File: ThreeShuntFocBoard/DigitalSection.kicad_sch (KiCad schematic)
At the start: 16 parts, among them J1 Conn_01x05, J2 Conn_02x03_Odd_Even, J5 Conn_01x05

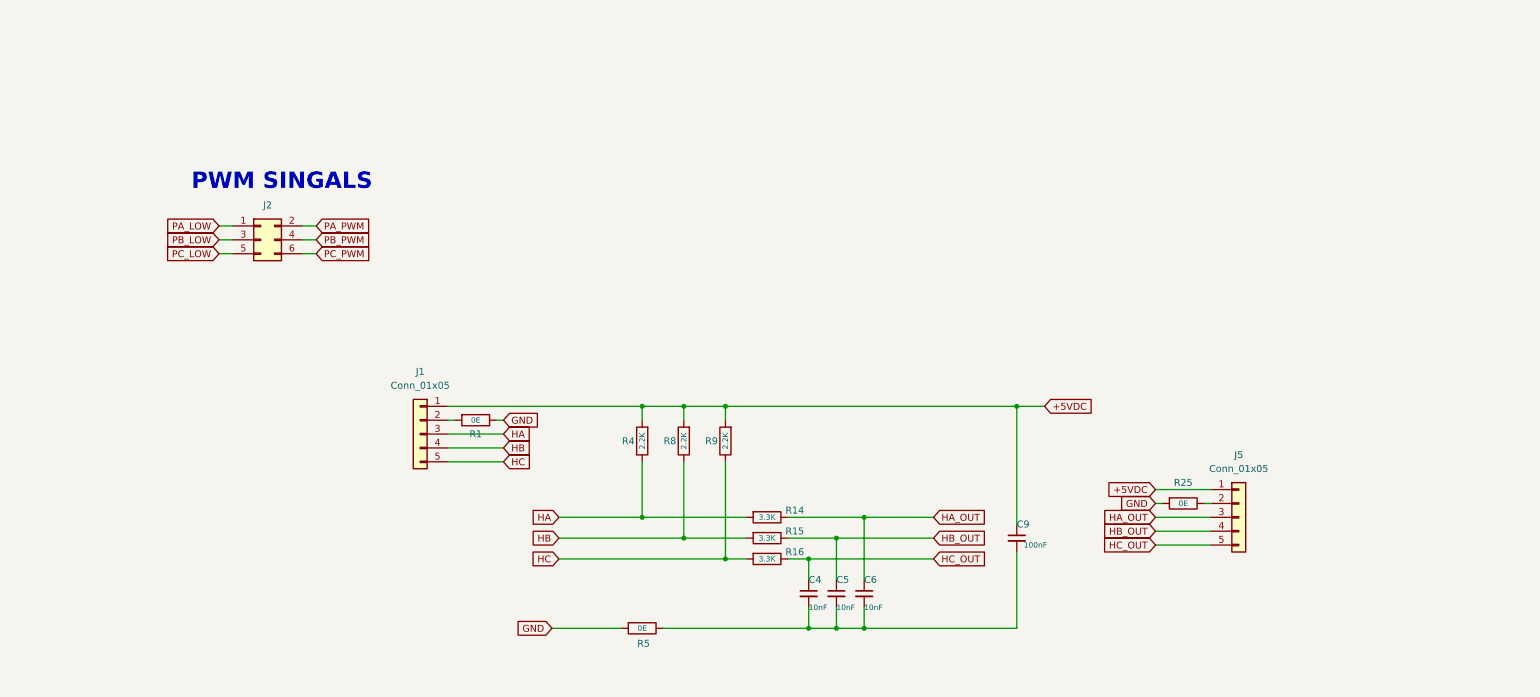
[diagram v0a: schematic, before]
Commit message: commit 2:  Updated Power Supply, Safety Fuse, Phase Design, and Hall Sensor Circuit
for more details read ChangesDetial.txt in same folder.
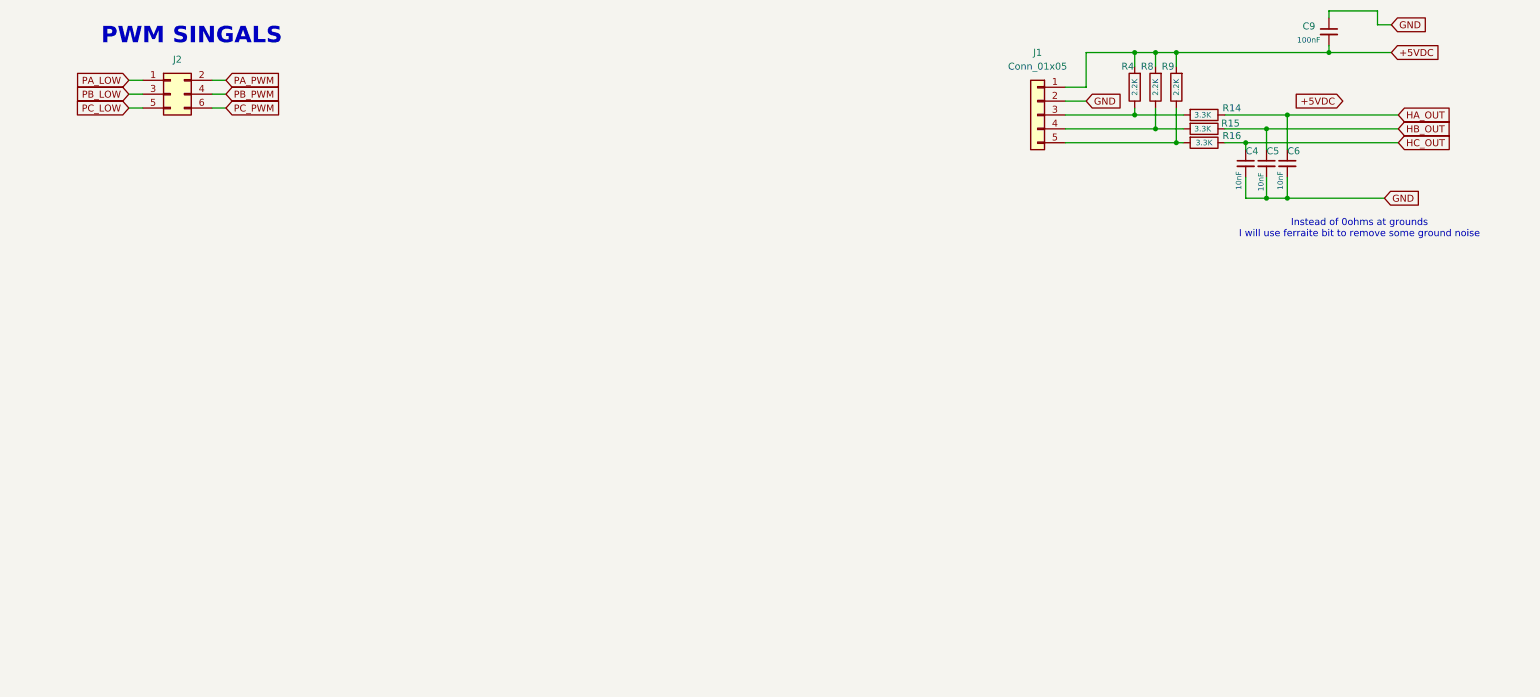
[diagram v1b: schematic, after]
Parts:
- removed J5: Conn_01x05, BLDC:Socket_Strip_Straight_1x05_Pitch2.54mm, symbol Connector_Generic:Conn_01x05
- removed R1, R25, R5: 0E, Footprints:R_0603, symbol Device:R
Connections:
- net +5VDC: now also C9.2; no longer C9.1
- net GND: now also C4.2, C5.2, C6.2, C9.1, J1.2 (Pin_2)
- net HA: no longer names the net of J1.3 (Pin_3), R14.2, R4.1
- net HB: no longer names the net of J1.4 (Pin_4), R15.2, R8.1
- net HC: no longer names the net of J1.5 (Pin_5), R16.2, R9.1
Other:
- note added: "Instead of 0ohms at grounds I will use ferraite bit to remove some ground noise"
- moved on the sheet: C4, C5, C6, C9, J1, J2, R14, R15, R16, R4, R8, R9

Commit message: Commit 3: Assigned STM32G431C6Tx (LQFP-48) pins as per the shared Excel, peripheral connections WIP, Phase C current sensing removed due to ADC group limitations
read attach excel files and changesDetails.txt file for more detail
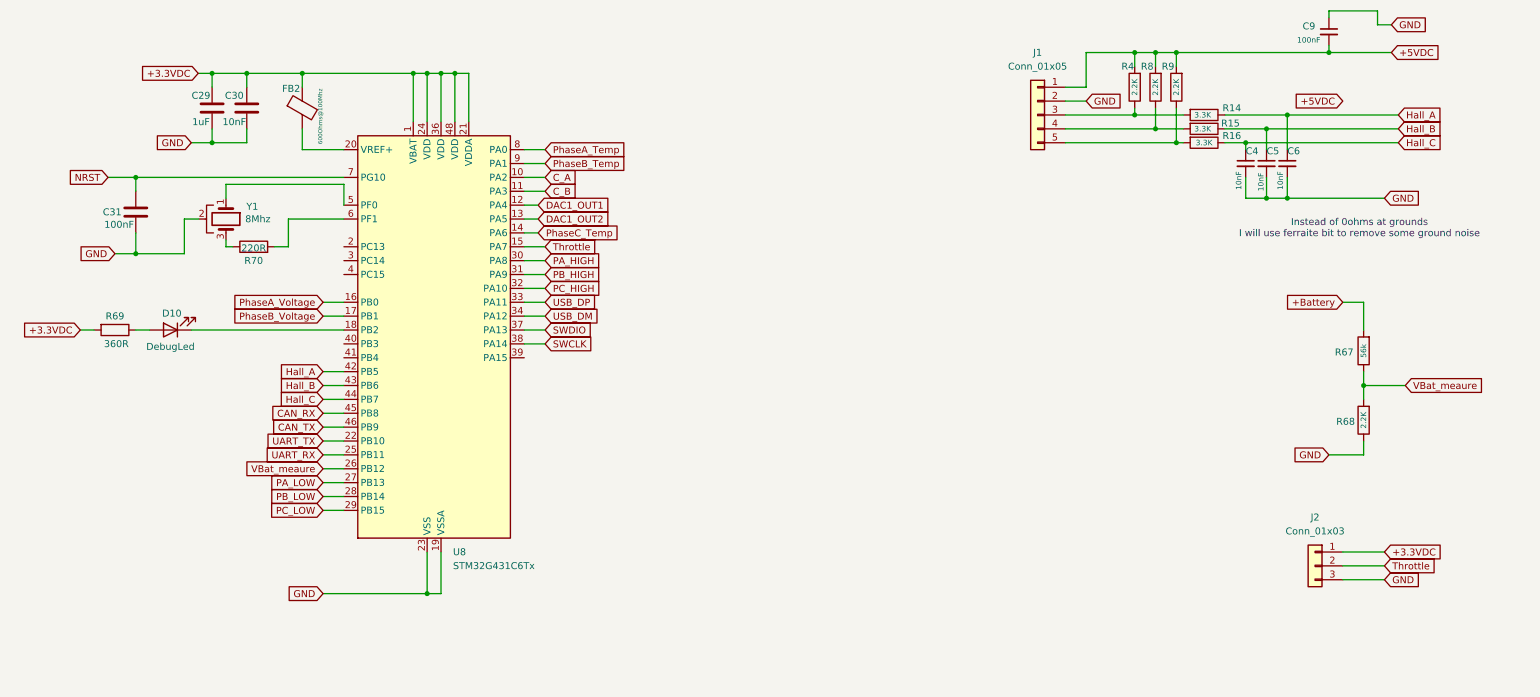
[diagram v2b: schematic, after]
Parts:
- removed J2: Conn_02x03_Odd_Even, BLDC:Socket_Strip_Straight_oddeven_2x06_Pitch2.54mm, symbol Connector_Generic:Conn_02x03_Odd_Even
- added C29: 1uF, symbol Device:C
- added C30: 10nF, symbol Device:C
- added C31: 100nF, symbol Device:C
- added D10: DebugLed, symbol Device:LED
- added FB2: 600Ohms@100Mhz, symbol Device:FerriteBead
- added J2: Conn_01x03, symbol Connector_Generic:Conn_01x03
- added R67: 56k, Footprints:R_0603, symbol Device:R
- added R68: 2.2K, Footprints:R_0603, symbol Device:R
- added R69: 360R, symbol Device:R
- added R70: 220R, symbol Device:R
- added U8: STM32G431C6Tx, Package_QFP:LQFP-48_7x7mm_P0.5mm, symbol MCU_ST_STM32G4:STM32G431C6Tx
- added Y1: 8Mhz, symbol Device:Crystal_GND2
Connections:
- net GND: now also C29.1, C30.1, C31.1, J2.3 (Pin_3), R68.1, U8.19 (VSSA), U8.23 (VSS), U8.35 (VSS), U8.47 (VSS), Y1.2
- net PA_LOW: now also U8.27 (PB13)
- net PB_LOW: now also U8.28 (PB14)
- net PC_LOW: now also U8.29 (PB15)
- net HA_OUT renamed Hall_A
- net Hall_A: now also U8.42 (PB5)
- net HB_OUT renamed Hall_B
- net Hall_B: now also U8.43 (PB6)
- net HC_OUT renamed Hall_C
- net Hall_C: now also U8.44 (PB7)
- new net: D10.1 (K), U8.18 (PB2)
- new net: D10.2 (A), R69.1
- new net: FB2.2, U8.20 (VREF+)
- new net: U8.5 (PF0), Y1.1
- new net: R70.2, U8.6 (PF1)
- new net: R70.1, Y1.3
- new net +3.3VDC: C29.2, C30.2, FB2.1, J2.1 (Pin_1), R69.2, U8.1 (VBAT), U8.21 (VDDA), U8.24 (VDD), U8.36 (VDD), U8.48 (VDD)
- new net +Battery: R67.2
- new net CAN_RX: U8.45 (PB8)
- new net CAN_TX: U8.46 (PB9)
- new net C_A: U8.10 (PA2)
- new net C_B: U8.11 (PA3)
- new net DAC1_OUT1: U8.12 (PA4)
- new net DAC1_OUT2: U8.13 (PA5)
- new net NRST: C31.2, U8.7 (PG10)
- new net PA_HIGH: U8.30 (PA8)
- new net PB_HIGH: U8.31 (PA9)
- new net PC_HIGH: U8.32 (PA10)
- new net PhaseA_Temp: U8.8 (PA0)
- new net PhaseA_Voltage: U8.16 (PB0)
- new net PhaseB_Temp: U8.9 (PA1)
- new net PhaseB_Voltage: U8.17 (PB1)
- new net PhaseC_Temp: U8.14 (PA6)
- new net SWCLK: U8.38 (PA14)
- new net SWDIO: U8.37 (PA13)
- new net Throttle: J2.2 (Pin_2), U8.15 (PA7)
- new net UART_RX: U8.25 (PB11)
- new net UART_TX: U8.22 (PB10)
- new net USB_DM: U8.34 (PA12)
- new net USB_DP: U8.33 (PA11)
- new net VBat_meaure: R67.1, R68.2, U8.26 (PB12)
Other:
- note removed: "PWM SINGALS"

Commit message: Commit 4: updated the schematic
Added crystal load capacitors, test points, SWO for debugging, PB8 as boot/CAN_RX, Pi filter on VDDA, and noted peripherals.
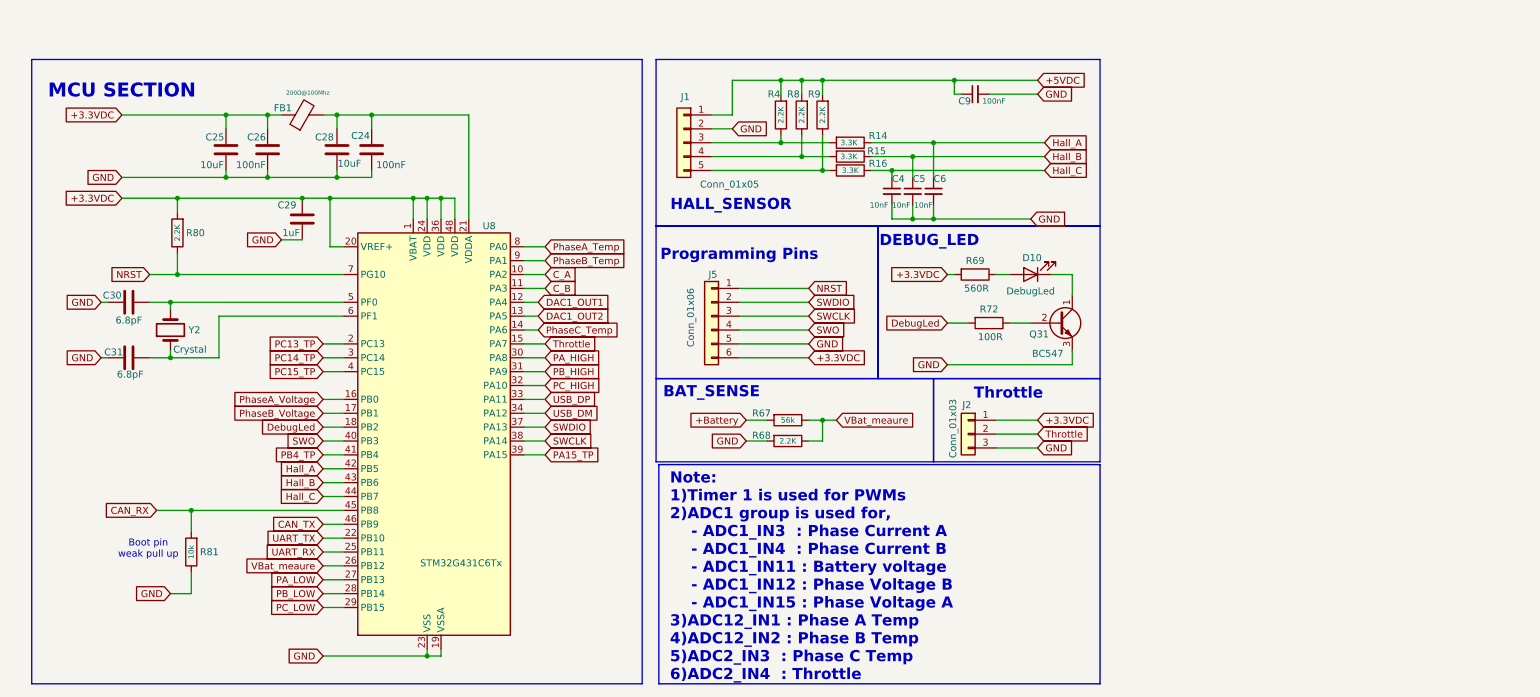
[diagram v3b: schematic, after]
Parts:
- removed FB2: 600Ohms@100Mhz, symbol Device:FerriteBead
- removed R70: 220R, symbol Device:R
- removed Y1: 8Mhz, symbol Device:Crystal_GND2
- added C24, C26: 100nF, symbol Device:C
- added C25, C28: 10uF, symbol Device:C
- added FB1: 200Ω@100Mhz, symbol Device:FerriteBead
- added J5: Conn_01x06, symbol Connector_Generic:Conn_01x06
- added Q31: BC547, Package_TO_SOT_THT:TO-92_Inline, symbol Transistor_BJT:BC547
- added R72: 100R, symbol Device:R
- added R80: 2.2K, Footprints:R_0603, symbol Device:R
- added R81: 10k, Footprints:R_0603, symbol Device:R
- added Y2: Crystal, symbol Device:Crystal
- C30: value 10nF -> 6.8pF
- C31: value 100nF -> 6.8pF
- R69: value 360R -> 560R
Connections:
- net +3.3VDC: now also U8.20 (VREF+), C25.2, C26.2, FB1.1, J5.6 (Pin_6), R80.2; no longer C30.2, U8.21 (VDDA)
- net +5VDC: now also C9.1; no longer C9.2
- net CAN_RX: now also R81.2
- net GND: now also C30.2, C31.2, C9.2, R68.2, C24.1, C25.1, C26.1, C28.1, J5.5 (Pin_5), Q31.3 (E), R81.1; no longer C30.1, C31.1, C9.1, R68.1
- net NRST: now also J5.1 (Pin_1), R80.1; no longer C31.2
- net SWCLK: now also J5.3 (Pin_3)
- net SWDIO: now also J5.2 (Pin_2)
- net VBat_meaure: now also R68.1; no longer R68.2
- net at D10.1 (K): now also Q31.1 (C); no longer U8.18 (PB2)
- net PC13_TP: now reaches U8.2 (PC13)
- net PC14_TP: now reaches U8.3 (PC14)
- net PA15_TP: now reaches U8.39 (PA15)
- net PC15_TP: now reaches U8.4 (PC15)
- net SWO: now reaches U8.40 (PB3)
- net SWO: now also J5.4 (Pin_4)
- net PB4_TP: now reaches U8.41 (PB4)
- net at U8.5 (PF0): now also C30.1, Y2.2
- net at U8.6 (PF1): now also C31.1, Y2.1
- new net: C24.2, C28.2, FB1.2, U8.21 (VDDA)
- new net: Q31.2 (B), R72.1
- new net DebugLed: R72.2, U8.18 (PB2)
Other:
- note added: "BAT_SENSE"
- note added: "Boot pin weak pull up"
- note added: "DEBUG_LED"
- note added: "HALL_SENSOR"
- note added: "MCU SECTION"
- note added: "Note: 1)Timer 1 is used for PWMs 2)ADC1 group is used for, - ADC1_IN3 : Phase Current A - ADC1_IN4 : Phase Current B - ADC1_IN11 : Battery voltage - ADC1_IN12 : Phase Voltage B - ADC1_IN15 : Phase Voltage A 3)ADC12_IN1 : Phase A Temp 4)ADC12_IN2 : Phase B Temp 5)ADC2_IN3 : Phase C Temp 6)ADC2_IN4 : Throttle"
- note added: "Programming Pins"
- note added: "Throttle"
- note removed: "Instead of 0ohms at grounds I will use ferraite bit to remove some ground noise"
- moved on the sheet: C29, C4, C5, C6, C9, D10, J1, J2, R14, R15, R16, R4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

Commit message: Commit 5: Improved power integrity and ADC accuracy.
for more details read changesDetail.txt file
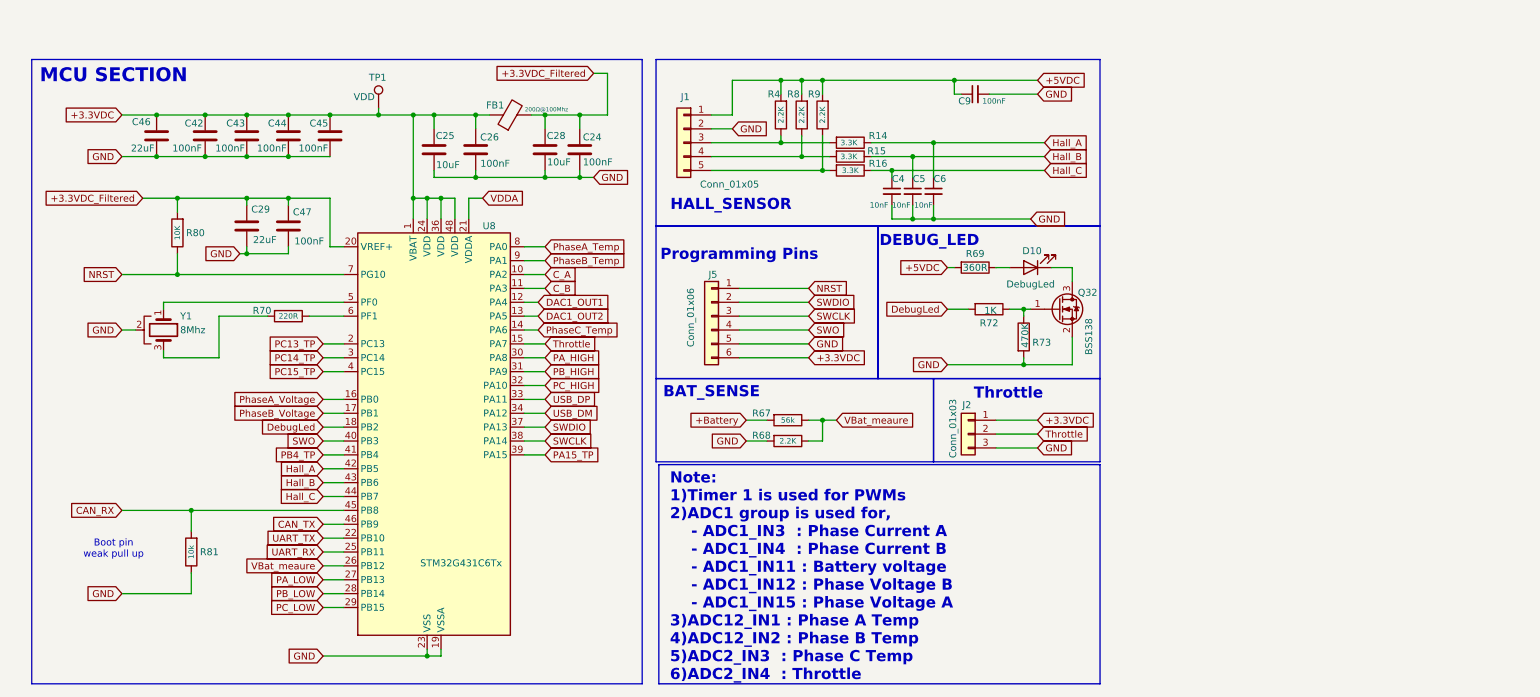
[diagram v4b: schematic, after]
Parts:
- removed C30, C31: 6.8pF, symbol Device:C
- removed Q31: BC547, Package_TO_SOT_THT:TO-92_Inline, symbol Transistor_BJT:BC547
- removed Y2: Crystal, symbol Device:Crystal
- added C42, C43, C44, C45, C47: 100nF, symbol Device:C
- added C46: 22uF, symbol Device:C
- added Q32: BSS138, Package_TO_SOT_SMD:SOT-23, symbol Transistor_FET:BSS138
- added R70: 220R, Footprints:R_0603, symbol Device:R
- added R73: 470K, symbol Device:R
- added TP1: VDD, symbol Connector:TestPoint
- added Y1: 8Mhz, symbol Device:Crystal_GND2
- C29: value 1uF -> 22uF
- R69: value 560R -> 360R
- R72: value 100R -> 1K
- R80: value 2.2K -> 10K
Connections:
- net +3.3VDC: now also C42.2, C43.2, C44.2, C45.2, C46.2, TP1.1; no longer C29.2, R69.2, R80.2, U8.20 (VREF+)
- net +5VDC: now also R69.2
- net GND: now also C42.1, C43.1, C44.1, C45.1, C46.1, C47.1, Q32.2 (S), R73.2, Y1.2
- net at D10.1 (K): now also Q32.3 (D)
- net +3.3VDC_Filtered: now reaches C24.2, C28.2, FB1.2
- net +3.3VDC_Filtered: now also C29.2, R80.2, U8.20 (VREF+), C47.2; no longer U8.21 (VDDA)
- net at U8.5 (PF0): now also Y1.1
- net at U8.6 (PF1): now also R70.1
- net at R72.1: now also Q32.1 (G), R73.1
- new net: R70.2, Y1.3
- new net VDDA: U8.21 (VDDA)
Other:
- moved on the sheet: C24, C25, C26, C28, C29, D10, FB1, R69, R72
